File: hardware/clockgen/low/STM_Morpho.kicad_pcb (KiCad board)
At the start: 2 copper layers, 70 x 95.8 mm, 13 parts, among them CN10 Conn_02x19_Odd_Even, CN7 Conn_02x19_Odd_Even, J1 Conn_02x20_Odd_Even, U1 74ALVC164245DLG4, U2 74ALVC164245DLG4

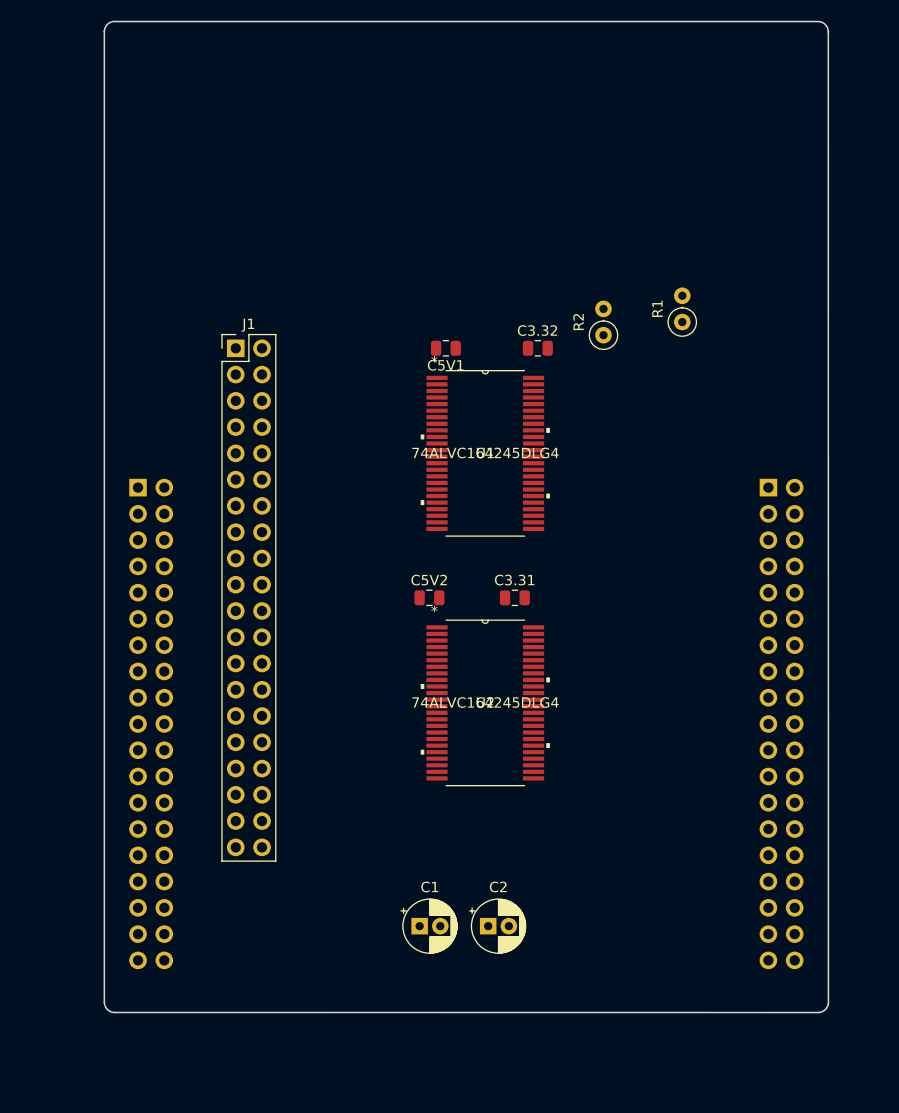
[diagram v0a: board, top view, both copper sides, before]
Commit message: Two PCBs are routed
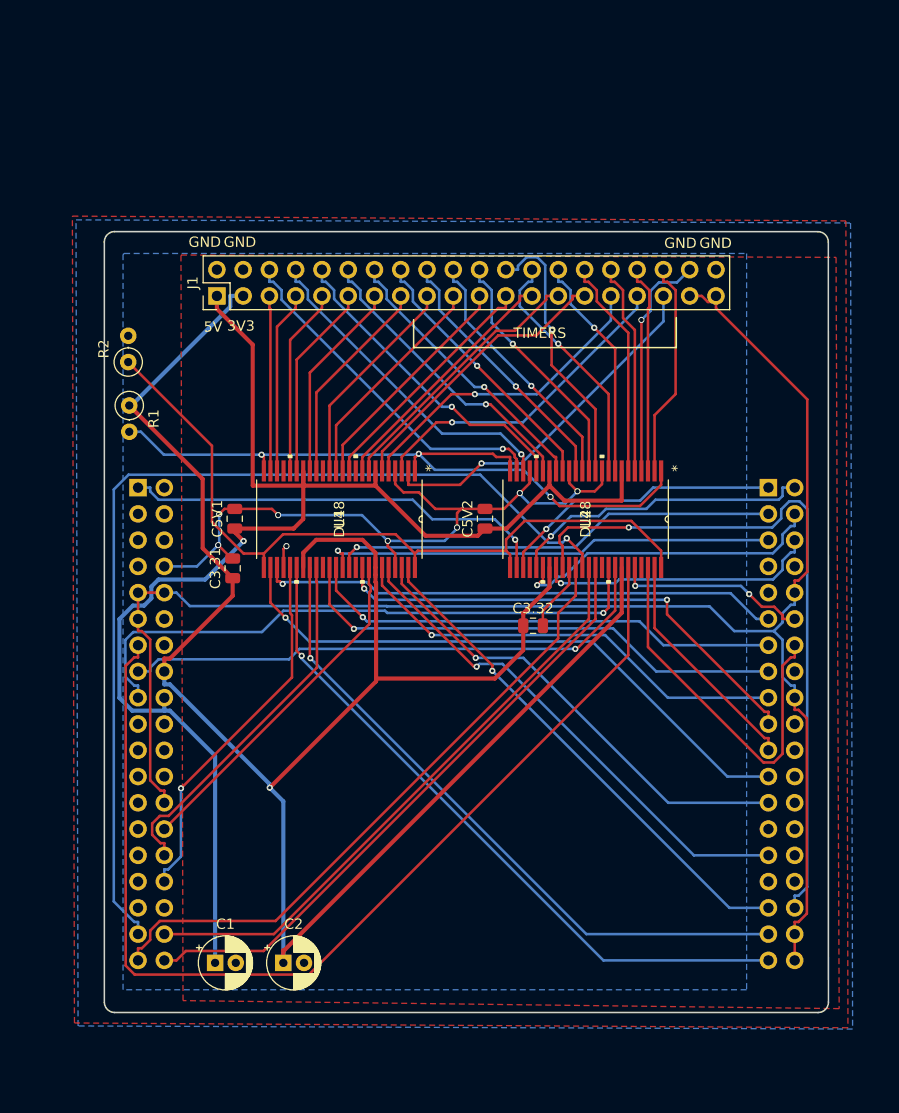
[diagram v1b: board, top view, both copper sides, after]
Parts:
- U1, U2: value 74ALVC164245DLG4 -> DL48
- moved R1 54.1 mm to (132.4, 63.3), turned to 270 degrees
- moved R2 46.0 mm to (132.3, 59.1)
- moved C3.31 27.4 mm to (142.4, 79.0), turned to 90 degrees
- moved C3.32 26.8 mm to (171.4, 84.6)
- moved C5V1 26.2 mm to (142.6, 74.2), turned to 90 degrees
- moved U2 20.2 mm to (176.5, 74.3), turned to 270 degrees
- moved C2 20.1 mm to (147.3, 117.2)
- moved C1 20.1 mm to (140.7, 117.2)
- moved U1 15.5 mm to (152.7, 74.3), turned to 270 degrees
- moved C5V2 9.35 mm to (166.8, 74.2), turned to 90 degrees
- moved J1 5.38 mm to (140.9, 52.7), turned to 90 degrees
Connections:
- J1 pad 10: /PB9_5V -> /PC8_5V
- J1 pad 11: /PA6_5V -> /PA3_5V
- J1 pad 12: /PA7_5V -> /PC6_5V
- J1 pad 13: /PA1_5V -> /PA2_5V
- J1 pad 14: /PA2_5V -> /PC5_5V
- J1 pad 15: /PA3_5V -> /PA1_5V
- J1 pad 16: /PA4_5V -> /PC4_5V
- J1 pad 17: /PA5_5V -> /PA7_5V
- J1 pad 18: /PA8_5V -> /PC3_5V
- J1 pad 19: /NC -> /PA6_5V
- J1 pad 2: +3V3 -> GND
- J1 pad 20: /NC -> /PC2_5V
- J1 pad 21: GND -> /PB9_5V
- J1 pad 22: GND -> /PC1_5V
- J1 pad 23: /PA9_5V -> /PB8_5V
- J1 pad 24: /PA11_5V -> /PC0_5V
- J1 pad 25: /PA12_5V -> /PC7_5V
- J1 pad 26: /PA13_5V -> /PA15_5V
- J1 pad 27: /PA14_5V -> /PA0_5V
- J1 pad 28: /PA15_5V -> /PA14_5V
- J1 pad 29: /PC0_5V -> /PB6_5V
- J1 pad 3: /PA10_5V -> +3V3
- J1 pad 30: /PC1_5V -> /PA13_5V
- J1 pad 31: /PC2_5V -> /PB5_5V
- J1 pad 32: /PC3_5V -> /PA12_5V
- J1 pad 33: /PC4_5V -> /PB10_5V
- J1 pad 34: /PC5_5V -> /PA11_5V
- J1 pad 35: /PC6_5V -> /PA10_5V
- J1 pad 36: /PC8_5V -> /PA9_5V
- J1 pad 37: /PC9_5V -> /NC
- J1 pad 38: /PC10_5V -> GND
- J1 pad 39: GND -> /NC
- J1 pad 4: /PB10_5V -> GND
- J1 pad 5: /PB5_5V -> /PA8_5V
- J1 pad 6: /PB6_5V -> /PC10_5V
- J1 pad 7: /PA0_5V -> /PA5_5V
- J1 pad 8: /PC7_5V -> /PC9_5V
- J1 pad 9: /PB8_5V -> /PA4_5V
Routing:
- net +3V3: track 0.00 -> 194.9 mm, vias 0 -> 1
- net /NC: track 0.00 -> 159.7 mm
- net +5V: track 0.00 -> 136.7 mm, vias 0 -> 1
- net GND: track 0.00 -> 102.6 mm, vias 0 -> 9
- net /PA13: track 0.00 -> 101.9 mm
- net /PC2: track 0.00 -> 94.9 mm, vias 0 -> 1
- net /PULLDOWN: track 0.10 -> 74.3 mm
- net /PULLUP: track 0.00 -> 70.5 mm, vias 0 -> 3
- net /PC4: track 0.00 -> 68.6 mm, vias 0 -> 1
- net /PA3: track 0.00 -> 66.2 mm, vias 0 -> 1
- net /PA2: track 0.00 -> 64.1 mm, vias 0 -> 1
- net /PC3: track 0.00 -> 62.3 mm
- net /PC0: track 0.00 -> 60.4 mm
- net /PC1: track 0.00 -> 58.7 mm
- net /PA8: track 0.00 -> 58.5 mm, vias 0 -> 1
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- added copper zone on B.Cu, net (none)
- added copper zone on F.Cu, net (none)
- added copper zone on B.Cu, net GND
- added copper zone on F.Cu, net GND
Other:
- board size 70 x 95.8 mm -> 70 x 75.5 mm
- net class HighPower: trace_width 0.5 -> 0.4
- net class Power: trace_width 0.35 -> 0.3
- board text added: "3V3"
- board text added: "5V"
- board text added: "GND"
- board text added: "TIMERS"

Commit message: Screw terminal adapter added
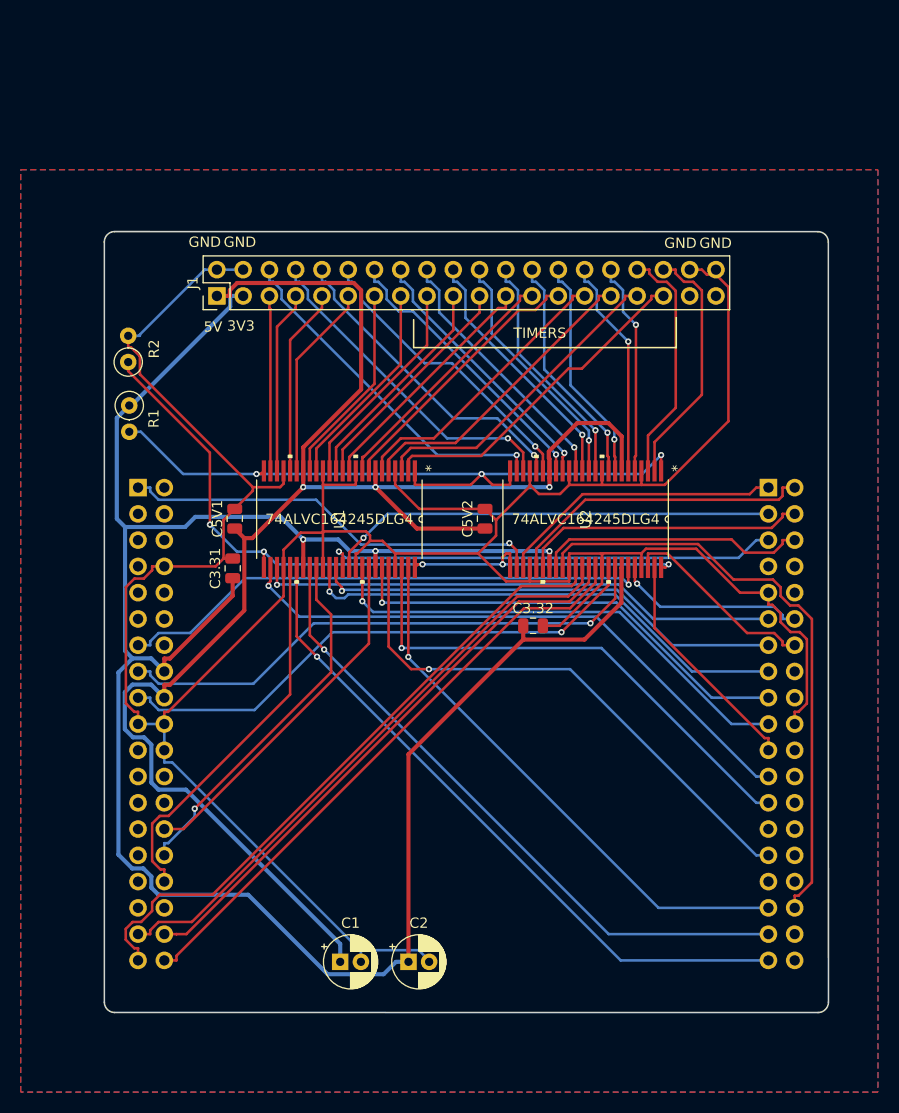
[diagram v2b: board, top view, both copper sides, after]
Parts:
- U1, U2: value DL48 -> 74ALVC164245DLG4
- moved C1 12.1 mm to (152.8, 117.1)
- moved C2 12.1 mm to (159.4, 117.1)
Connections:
- CN10 pad 10: /NC -> (no net)
- CN10 pad 18: /NC -> (no net)
- CN10 pad 36: /NC -> (no net)
- CN10 pad 38: /NC -> (no net)
- CN7 pad 10: /NC -> (no net)
- CN7 pad 11: /NC -> (no net)
- CN7 pad 26: /NC -> (no net)
- CN7 pad 9: /NC -> (no net)
- J1 pad 37: /NC -> (no net)
- J1 pad 39: /NC -> (no net)
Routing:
- net GND: track 102.6 -> 303.1 mm, vias 9 -> 0
- net /NC: track 159.7 -> 0.00 mm
- net /PA13: track 101.9 -> 52.3 mm, vias 0 -> 1
- net /PC2: track 94.9 -> 58.7 mm, vias 1 -> 0
- net +5V: track 136.7 -> 159.2 mm, vias 1 -> 3
- net /PA11: track 36.9 -> 19.4 mm
- net +3V3: track 194.9 -> 211.0 mm, vias 1 -> 3
- net /PC4: track 68.6 -> 58.2 mm, vias 1 -> 0
- net /PA15: track 58.4 -> 52.9 mm
- net /PA10: track 49.6 -> 53.6 mm
- net /PB10: track 45.8 -> 49.5 mm
- net /PC0_5V: track 26.8 -> 23.3 mm
- net /PB5: track 49.3 -> 52.7 mm
- net /PC6: track 31.0 -> 27.7 mm, vias 1 -> 0
- net /PULLDOWN: track 74.3 -> 71.1 mm, vias 0 -> 5
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- removed copper zone on B.Cu, net (none)
- removed copper zone on F.Cu, net (none)
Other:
- net class HighPower: trace_width 0.4 -> 0.5
